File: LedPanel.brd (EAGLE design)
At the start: 100 x 100 mm, 13 parts, among them U1 AL8805W5-7

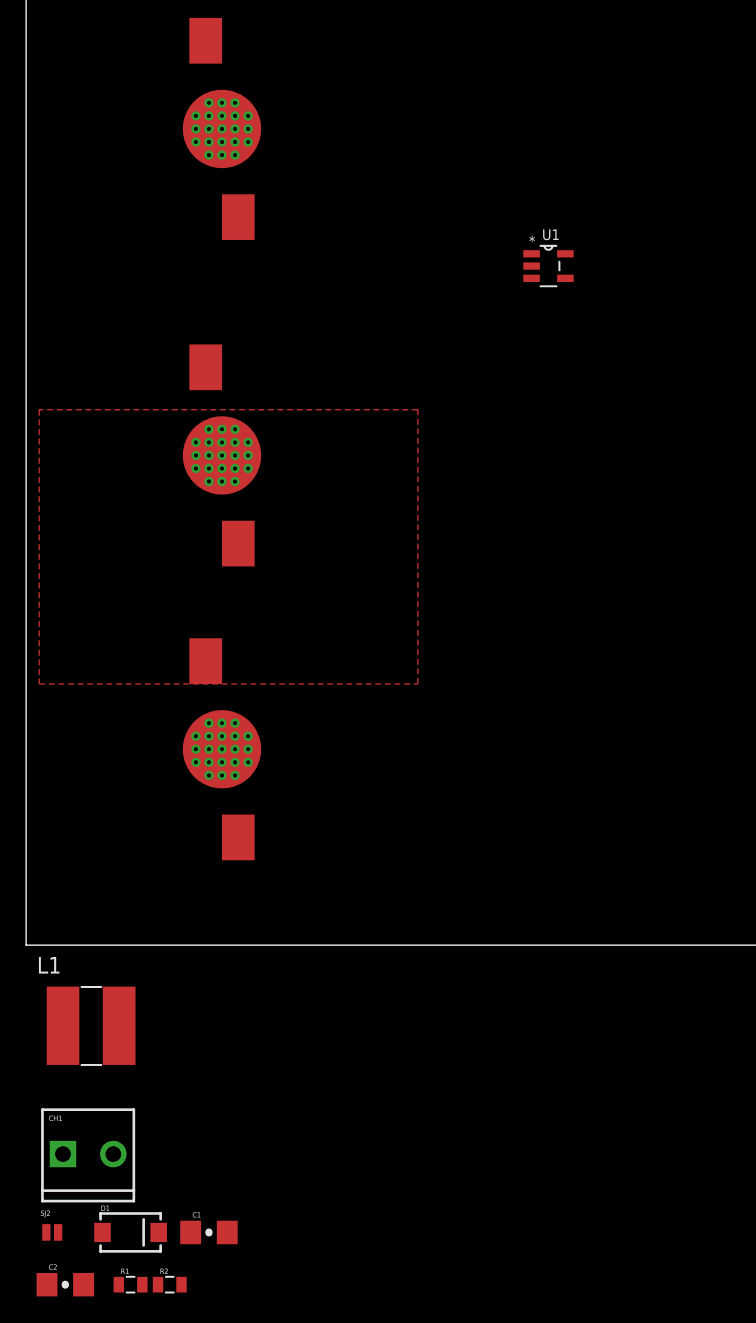
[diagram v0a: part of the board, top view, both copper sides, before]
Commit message: Connecting the led driver, fixing some issues
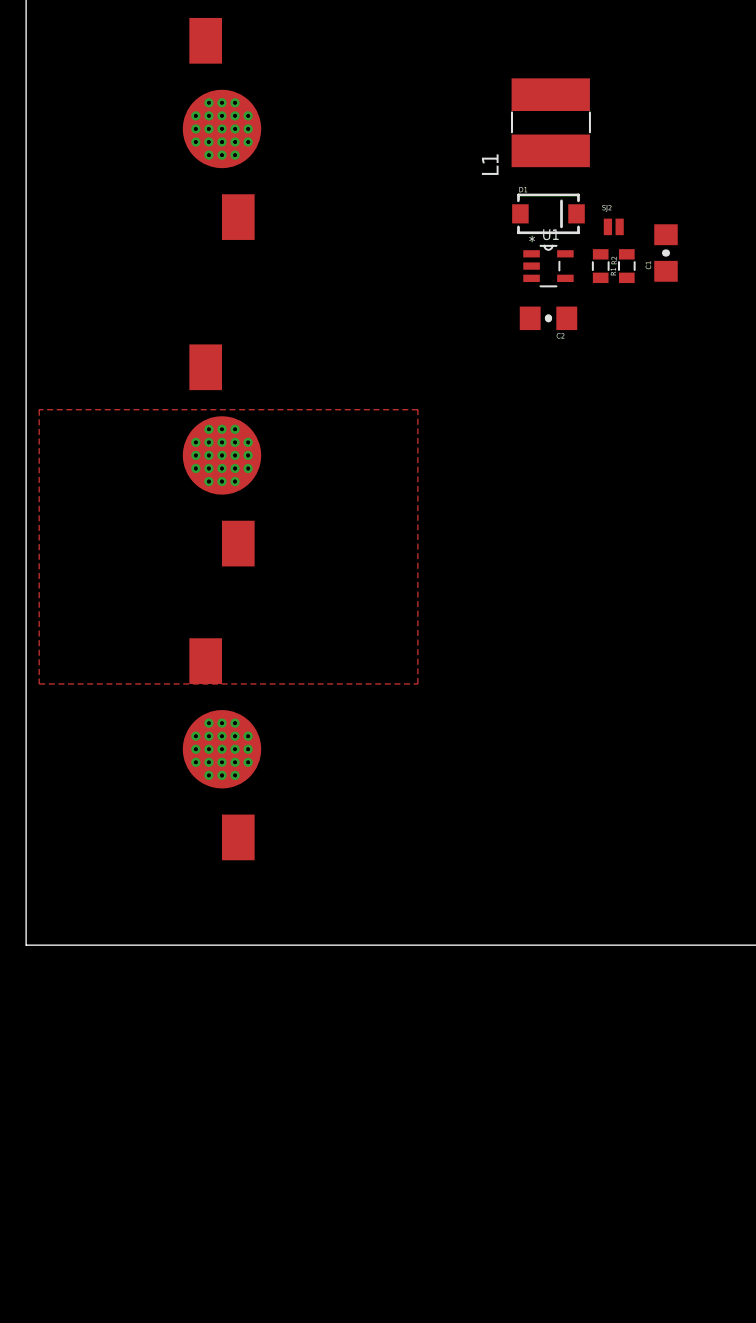
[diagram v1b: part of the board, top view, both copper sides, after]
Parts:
- removed CH1: (no value), SparkFun:SCREWTERMINAL-3.5MM-2_LOCK
- moved SJ2 88.2 mm to (45.0, 55.0)
- moved R1 86.8 mm to (46.0, 52.0), turned to 90 degrees
- moved R2 84.7 mm to (44.0, 52.0), turned to 270 degrees
- moved D1 84.3 mm to (40.0, 56.0)
- moved C1 82.8 mm to (49.0, 53.0), turned to 90 degrees
- moved C2 82.7 mm to (40.0, 48.0), turned to 180 degrees
- moved L1 77.4 mm to (40.0, 63.0), turned to 90 degrees
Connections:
- removed net N$4: U$4.CATHODE
- removed net N$5: U$1.ANODE, U$1.P$1, U$1.P$10, U$1.P$11, U$1.P$12, U$1.P$13, U$1.P$14, U$1.P$15, U$1.P$16, U$1.P$17, U$1.P$18, U$1.P$19, U$1.P$2, U$1.P$20, U$1.P$21, U$1.P$3, U$1.P$4, U$1.P$5, U$1.P$6, U$1.P$7, U$1.P$8, U$1.P$9, U$1.SLUG
- removed net OUT+: C1.1, CH1.2, R1.1, R2.2
- removed net OUT-: C1.2, CH1.1, L1.2
- removed net VIN: C2.1, D1.C, R2.1, SJ2.1
- new net LED1_OUT+: C1.1, R1.1, R2.2, U$1.ANODE, U$1.P$1, U$1.P$10, U$1.P$11, U$1.P$12, U$1.P$13, U$1.P$14, U$1.P$15, U$1.P$16, U$1.P$17, U$1.P$18, U$1.P$19, U$1.P$2, U$1.P$20, U$1.P$21, U$1.P$3, U$1.P$4, U$1.P$5, U$1.P$6, U$1.P$7, U$1.P$8, U$1.P$9, U$1.SLUG, U1.4
- new net LED1_OUT-: C1.2, L1.2, U$4.CATHODE
- net SW: now also U1.1
- net VCC: now also C2.1, D1.C, R2.1, SJ2.1

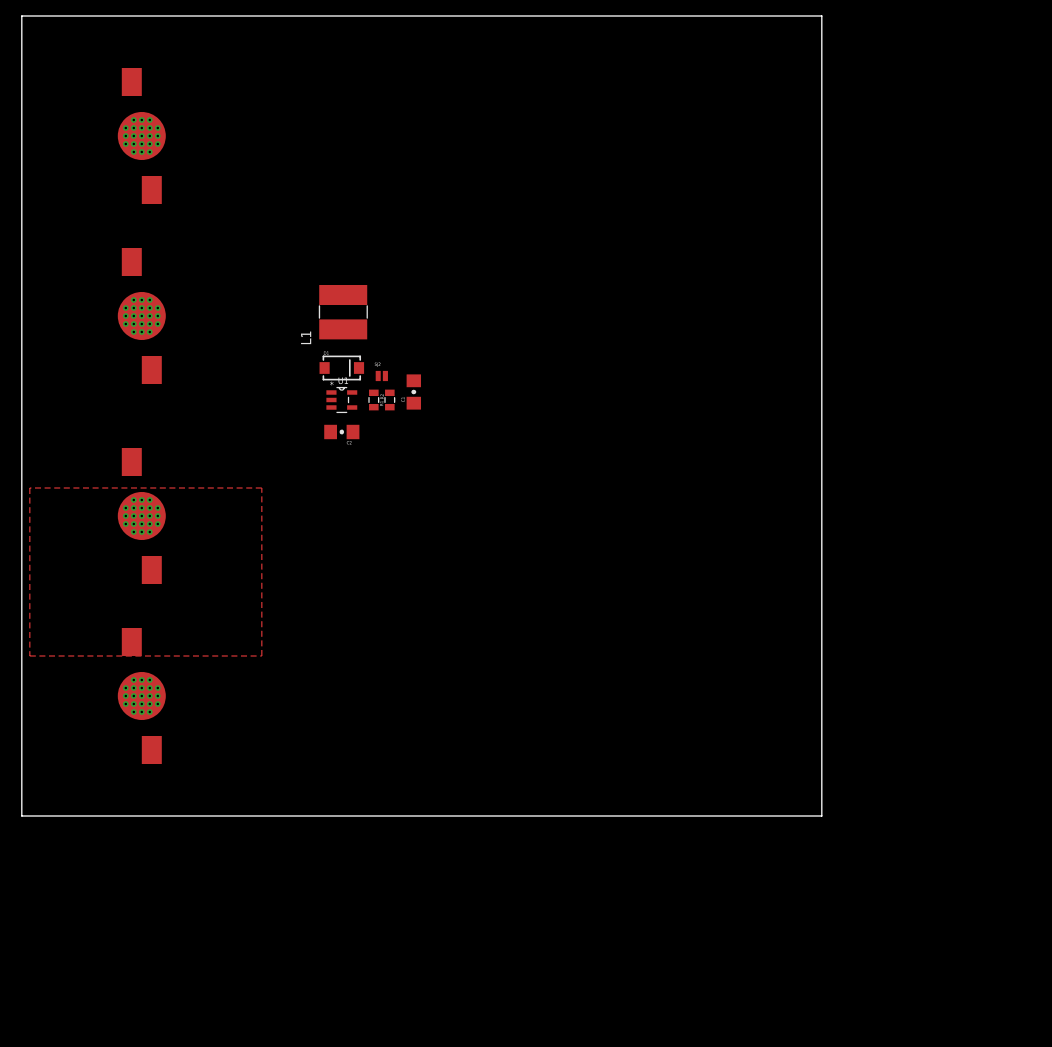
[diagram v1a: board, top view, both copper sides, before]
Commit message: Creating 3 string of 4 leds. 12 3W leds in total. Peak power is 36W?
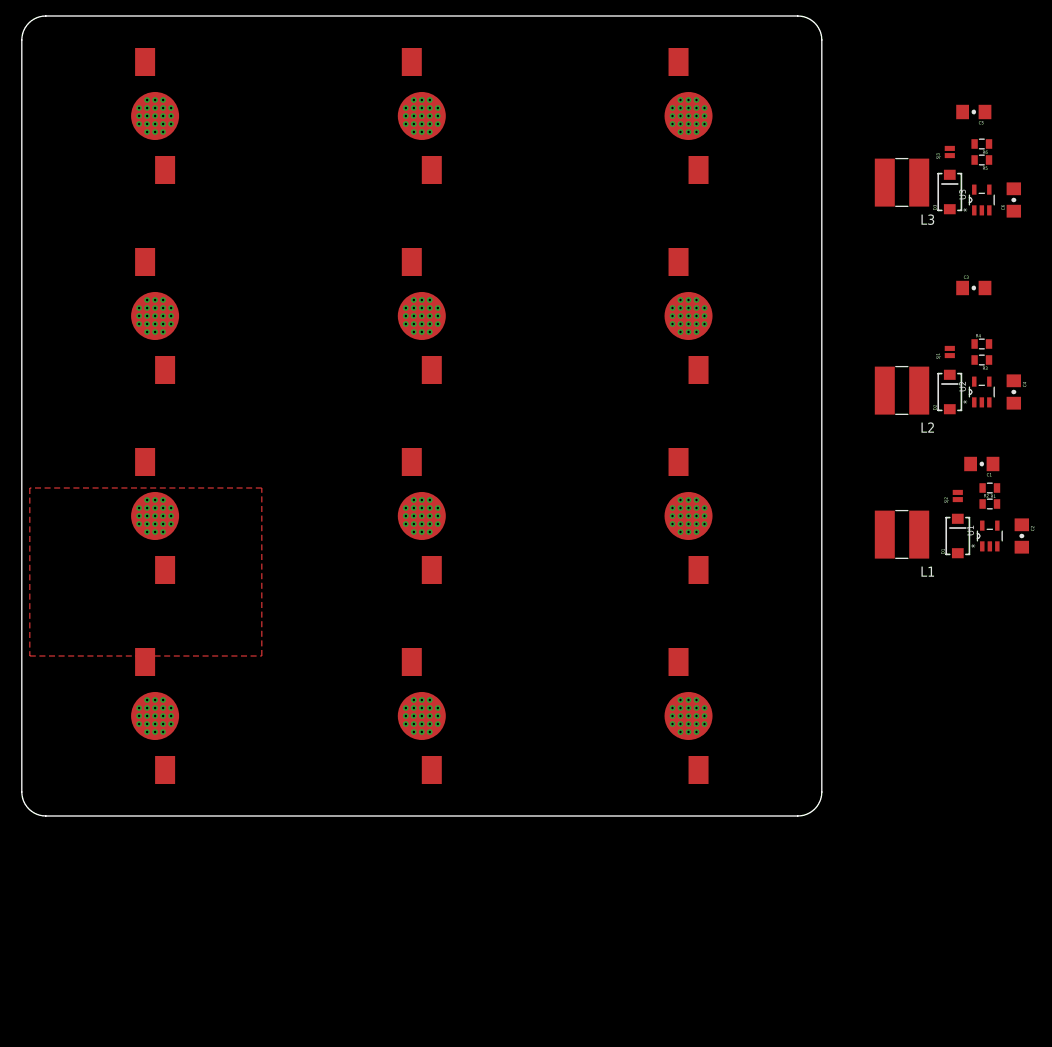
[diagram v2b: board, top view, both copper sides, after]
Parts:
- added C3, C5: 1uF, SparkFun-Capacitors:1206-CAP
- added C4, C6: 2.2uF, SparkFun-Capacitors:1206-CAP
- added D2, D3: MBRA140, SparkFun-DiscreteSemi:SMA-DIODE
- added L2, L3: 33uH, SparkFun-Passives:SRN6045
- added R3, R4, R5, R6: 0.3R, SparkFun-Resistors:0805
- added SJ1, SJ3: NO Jumper, SparkFun-Passives:PAD-JUMPER-2-NO_NO_SILK
- added U$10, U$11, U$12, U$5, U$6, U$7, U$8, U$9: LED_3W, LedPanel:LED_3W
- added U2, U3: AL8805W5-7, LedPanel:SOT95P280X130-5N
- moved C2 86.0 mm to (125.0, 35.0), turned to 270 degrees
- moved U1 82.8 mm to (121.0, 35.0), turned to 90 degrees
- moved D1 79.8 mm to (117.0, 35.0), turned to 90 degrees
- moved R2 78.1 mm to (121.0, 39.0), turned to 0 degrees
- moved R1 75.8 mm to (121.0, 41.0), turned to 180 degrees
- moved L1 75.4 mm to (110.0, 35.0), turned to 180 degrees
- moved SJ2 73.5 mm to (117.0, 40.0), turned to 90 degrees
- moved C1 71.6 mm to (120.0, 44.0), turned to 180 degrees
- moved U$1 3.00 mm to (16.7, 12.5)
- moved U$4 3.00 mm to (16.7, 87.5)
- moved U$2 1.66 mm to (16.7, 37.5)
- moved U$3 1.66 mm to (16.7, 62.5)
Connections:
- net SW renamed SW1
- new net LED2_OUT+: C3.1, R3.1, R4.2, U$5.ANODE, U$5.P$1, U$5.P$10, U$5.P$11, U$5.P$12, U$5.P$13, U$5.P$14, U$5.P$15, U$5.P$16, U$5.P$17, U$5.P$18, U$5.P$19, U$5.P$2, U$5.P$20, U$5.P$21, U$5.P$3, U$5.P$4, U$5.P$5, U$5.P$6, U$5.P$7, U$5.P$8, U$5.P$9, U$5.SLUG, U2.4
- new net LED2_OUT-: C3.2, L2.2, U$8.CATHODE
- new net LED3_OUT+: C5.1, R5.1, R6.2, U$9.ANODE, U$9.P$1, U$9.P$10, U$9.P$11, U$9.P$12, U$9.P$13, U$9.P$14, U$9.P$15, U$9.P$16, U$9.P$17, U$9.P$18, U$9.P$19, U$9.P$2, U$9.P$20, U$9.P$21, U$9.P$3, U$9.P$4, U$9.P$5, U$9.P$6, U$9.P$7, U$9.P$8, U$9.P$9, U$9.SLUG, U3.4
- new net LED3_OUT-: C5.2, L3.2, U$12.CATHODE
- new net N$10: U$10.CATHODE, U$11.ANODE, U$11.P$1, U$11.P$10, U$11.P$11, U$11.P$12, U$11.P$13, U$11.P$14, U$11.P$15, U$11.P$16, U$11.P$17, U$11.P$18, U$11.P$19, U$11.P$2, U$11.P$20, U$11.P$21, U$11.P$3, U$11.P$4, U$11.P$5, U$11.P$6, U$11.P$7, U$11.P$8, U$11.P$9, U$11.SLUG
- new net N$11: U$10.ANODE, U$10.P$1, U$10.P$10, U$10.P$11, U$10.P$12, U$10.P$13, U$10.P$14, U$10.P$15, U$10.P$16, U$10.P$17, U$10.P$18, U$10.P$19, U$10.P$2, U$10.P$20, U$10.P$21, U$10.P$3, U$10.P$4, U$10.P$5, U$10.P$6, U$10.P$7, U$10.P$8, U$10.P$9, U$10.SLUG, U$9.CATHODE
- new net N$12: R5.2, SJ3.2
- new net N$4: U$7.CATHODE, U$8.ANODE, U$8.P$1, U$8.P$10, U$8.P$11, U$8.P$12, U$8.P$13, U$8.P$14, U$8.P$15, U$8.P$16, U$8.P$17, U$8.P$18, U$8.P$19, U$8.P$2, U$8.P$20, U$8.P$21, U$8.P$3, U$8.P$4, U$8.P$5, U$8.P$6, U$8.P$7, U$8.P$8, U$8.P$9, U$8.SLUG
- new net N$5: U$6.CATHODE, U$7.ANODE, U$7.P$1, U$7.P$10, U$7.P$11, U$7.P$12, U$7.P$13, U$7.P$14, U$7.P$15, U$7.P$16, U$7.P$17, U$7.P$18, U$7.P$19, U$7.P$2, U$7.P$20, U$7.P$21, U$7.P$3, U$7.P$4, U$7.P$5, U$7.P$6, U$7.P$7, U$7.P$8, U$7.P$9, U$7.SLUG
- new net N$7: U$5.CATHODE, U$6.ANODE, U$6.P$1, U$6.P$10, U$6.P$11, U$6.P$12, U$6.P$13, U$6.P$14, U$6.P$15, U$6.P$16, U$6.P$17, U$6.P$18, U$6.P$19, U$6.P$2, U$6.P$20, U$6.P$21, U$6.P$3, U$6.P$4, U$6.P$5, U$6.P$6, U$6.P$7, U$6.P$8, U$6.P$9, U$6.SLUG
- new net N$8: R3.2, SJ1.2
- new net N$9: U$11.CATHODE, U$12.ANODE, U$12.P$1, U$12.P$10, U$12.P$11, U$12.P$12, U$12.P$13, U$12.P$14, U$12.P$15, U$12.P$16, U$12.P$17, U$12.P$18, U$12.P$19, U$12.P$2, U$12.P$20, U$12.P$21, U$12.P$3, U$12.P$4, U$12.P$5, U$12.P$6, U$12.P$7, U$12.P$8, U$12.P$9, U$12.SLUG
- new net SW2: D2.A, L2.1, U2.1
- new net SW3: D3.A, L3.1, U3.1
- net GND: now also C4.2, C6.2, U2.2, U3.2
- net VCC: now also C4.1, C6.1, D2.C, D3.C, R4.1, R6.1, SJ1.1, SJ3.1, U2.5, U3.5
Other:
- outline, holes or cut-outs redrawn

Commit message: Adding ws8211 to control the leds
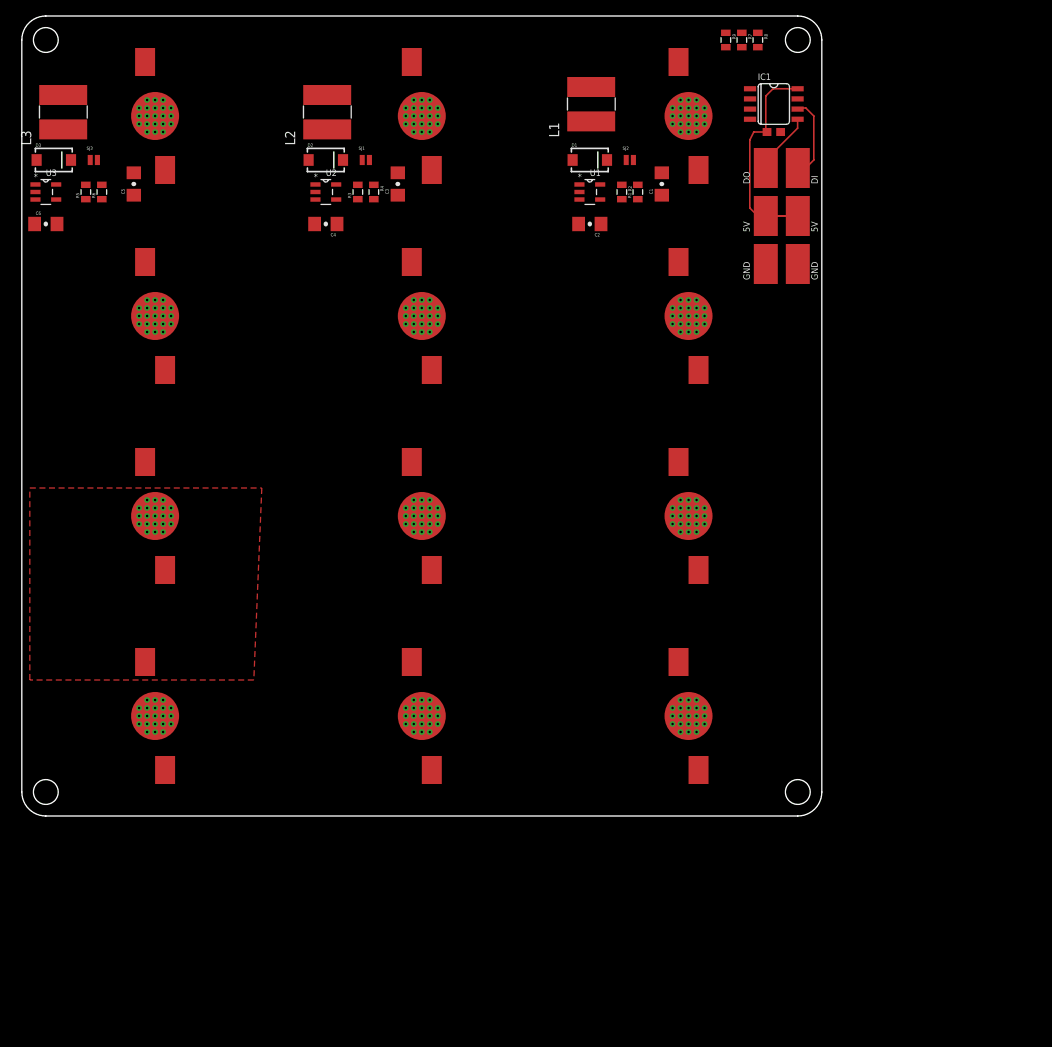
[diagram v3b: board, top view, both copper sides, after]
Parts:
- added 5V, U$16: 5V, LedPanel:SOLDER_PAD
- added DI: DI, LedPanel:SOLDER_PAD
- added DO: DO, LedPanel:SOLDER_PAD
- added IC1: WS2811-SOP8, LedPanel:SO08-SKINNYPADS
- added R7, R8, R9: 4.7k, SparkFun-Resistors:0805
- added U$15, U$18: GND, LedPanel:SOLDER_PAD
- moved C6 121.0 mm to (3.00, 74.0), turned to 0 degrees
- moved U3 117.0 mm to (3.00, 78.0), turned to 0 degrees
- moved D3 112.1 mm to (4.00, 82.0), turned to 0 degrees
- moved R5 112.1 mm to (8.00, 78.0), turned to 90 degrees
- moved R6 110.2 mm to (10.0, 78.0), turned to 90 degrees
- moved SJ3 107.0 mm to (9.00, 82.0), turned to 0 degrees
- moved C5 105.4 mm to (14.0, 79.0), turned to 90 degrees
- moved L3 105.4 mm to (5.00, 88.0), turned to 90 degrees
- moved C4 88.5 mm to (38.0, 74.0), turned to 180 degrees
- moved U2 85.7 mm to (38.0, 78.0), turned to 0 degrees
- moved D2 83.2 mm to (38.0, 82.0), turned to 0 degrees
- moved R3 80.8 mm to (42.0, 78.0), turned to 90 degrees
- moved L2 80.1 mm to (38.0, 88.0), turned to 90 degrees
- moved R4 78.3 mm to (44.0, 78.0), turned to 270 degrees
- moved SJ1 76.8 mm to (43.0, 82.0), turned to 0 degrees
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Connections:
- new net 5V: 5V.1, IC1.+5V, IC1.8, R7.1, R8.1, R9.1, U$16.1
- new net CTRL1: IC1.1, R7.2, U1.3
- new net CTRL2: IC1.2, R8.2, U2.3
- new net CTRL3: IC1.3, R9.2, U3.3
- new net N$13: DI.1, IC1.6
- new net N$14: DO.1, IC1.5
- net GND: now also IC1.4, IC1.GND, U$15.1, U$18.1
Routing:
- net 5V: track 0.00 -> 30.6 mm
- net N$13: track 0.00 -> 10.4 mm
- net N$14: track 0.00 -> 8.24 mm

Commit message: Layout first led driver
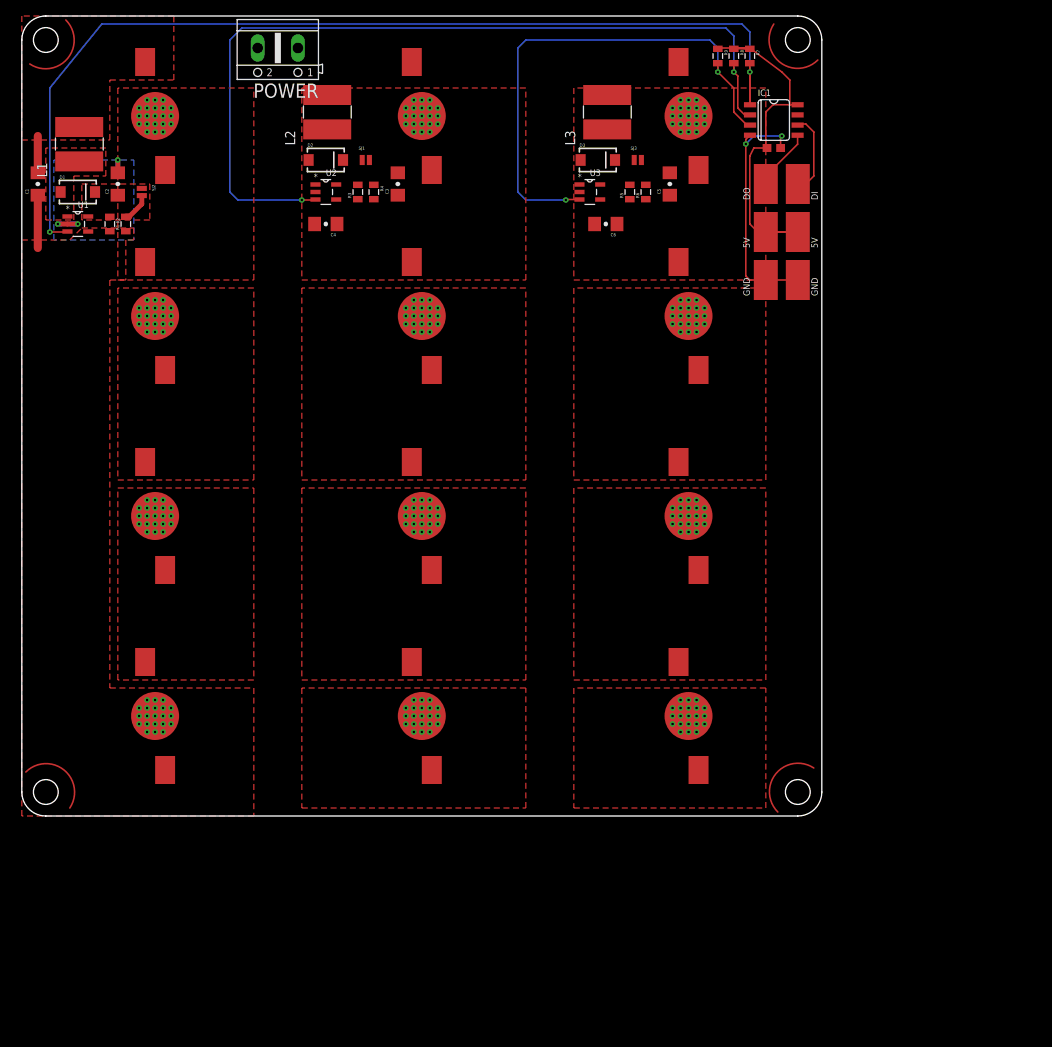
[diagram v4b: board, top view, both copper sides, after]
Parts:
- added POWER: (no value), LedPanel:AK500/2
- moved C1 78.0 mm to (2.00, 79.0)
- moved C6 70.0 mm to (73.0, 74.0), turned to 180 degrees
- moved D3 68.0 mm to (72.0, 82.0)
- moved L3 68.0 mm to (73.0, 88.0)
- moved R5 68.0 mm to (76.0, 78.0)
- moved R6 68.0 mm to (78.0, 78.0)
- moved SJ3 68.0 mm to (77.0, 82.0)
- moved U3 68.0 mm to (71.0, 78.0)
- moved C5 67.0 mm to (81.0, 79.0)
- moved L1 64.2 mm to (7.00, 84.0)
- moved D1 64.1 mm to (7.00, 78.0)
- moved R1 64.1 mm to (13.0, 74.0)
- moved R2 64.1 mm to (11.0, 74.0)
- moved U1 64.1 mm to (7.00, 74.0)
- moved SJ2 61.1 mm to (15.0, 78.0), turned to 270 degrees
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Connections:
- net GND: now also POWER.2
- net VCC: now also POWER.1
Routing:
- net CTRL1: track 0.00 -> 126.3 mm, vias 0 -> 2
- net CTRL2: track 0.00 -> 106.4 mm, vias 0 -> 2
- net CTRL3: track 0.00 -> 64.6 mm, vias 0 -> 2
- net GND: track 0.00 -> 37.6 mm, vias 0 -> 5
- net N$15: track 0.00 -> 28.4 mm
- net 5V: track 30.6 -> 50.0 mm
- net LED1_OUT+: track 0.00 -> 6.60 mm
- net LED1_OUT-: track 0.00 -> 4.60 mm
- net N$6: track 0.00 -> 3.71 mm
- added copper zone on layer 16, net GND
- added copper zone on layer 1, net LED1_OUT+
- added copper zone on layer 1, net LED1_OUT-
- added copper zone on layer 1, net LED2_OUT+
- added copper zone on layer 1, net LED3_OUT+
- added copper zone on layer 1, net N$1
- added copper zone on layer 1, net N$10
- added copper zone on layer 1, net N$11
- added copper zone on layer 1, net N$2
- added copper zone on layer 1, net N$4
- added copper zone on layer 1, net N$5
- added copper zone on layer 1, net N$7
- added copper zone on layer 1, net N$9
- added copper zone on layer 1, net SW1
- added copper zone on layer 1, net VCC

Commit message: Routing everything
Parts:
- moved C5 14.0 mm to (67.0, 78.0)
- moved C3 13.0 mm to (34.0, 78.0)
- moved C4 7.81 mm to (44.0, 79.0), turned to 90 degrees
- moved C6 6.40 mm to (77.0, 79.0), turned to 90 degrees
- moved SJ1 5.66 mm to (47.0, 78.0), turned to 270 degrees
- moved R3 5.00 mm to (45.0, 74.0)
- moved SJ3 5.00 mm to (80.0, 78.0), turned to 270 degrees
- moved R5 4.47 mm to (78.0, 74.0)
- moved R6 4.47 mm to (76.0, 74.0), turned to 270 degrees
- moved D2 4.12 mm to (39.0, 78.0)
- moved L2 4.12 mm to (39.0, 84.0)
- moved L3 4.12 mm to (72.0, 84.0)
- moved R4 4.12 mm to (43.0, 74.0)
- moved U2 4.12 mm to (39.0, 74.0)
- moved U3 4.12 mm to (72.0, 74.0)
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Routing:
- net GND: track 37.6 -> 58.5 mm, vias 5 -> 9
- net LED3_OUT-: track 0.00 -> 6.60 mm
- net LED2_OUT-: track 0.00 -> 6.60 mm
- net CTRL2: track 106.4 -> 99.9 mm, vias 2 -> 4
- net LED3_OUT+: track 0.00 -> 5.60 mm
- net LED2_OUT+: track 0.00 -> 5.60 mm
- net N$8: track 0.00 -> 3.48 mm
- net N$12: track 0.00 -> 3.48 mm
- net LED1_OUT-: track 4.60 -> 5.60 mm
- net LED1_OUT+: track 6.60 -> 5.60 mm
- net CTRL3: track 64.6 -> 64.8 mm, vias 2 -> 4
- added copper zone on layer 1, net LED2_OUT-
- added copper zone on layer 1, net LED3_OUT-
- added copper zone on layer 1, net SW2
- added copper zone on layer 1, net SW3
- added copper zone on layer 16, net VCC
